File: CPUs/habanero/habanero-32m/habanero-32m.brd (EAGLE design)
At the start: 63.4 x 25.4 mm, 38 parts, among them IC1 PIC32MX564F128H-80I/PT

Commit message: esto solo fue una prueba
rutee una inea dummy
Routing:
- net BUSON: track 9.04 -> 16.6 mm
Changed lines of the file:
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@@
 <?xml version="1.0" encoding="utf-8"?>
 <!DOCTYPE eagle SYSTEM "eagle.dtd">
-<eagle version="6.2">
+<eagle version="6.4">
 <drawing>
 <settings>
@@
 </class>
 </classes>
-<designrules>
+<designrules name="default">
 <description language="de">&lt;b&gt;EAGLE Design Rules&lt;/b&gt;
 &lt;p&gt;
@@
 <wire x1="18.4912" y1="8.128" x2="17.075" y2="8.128" width="0.2032" layer="1"/>
 <wire x1="17.075" y1="8.128" x2="17.004" y2="8.199" width="0.2032" layer="1"/>
-<wire x1="20.5" y1="11.75" x2="44.548625" y2="17.614390625" width="0" layer="19" extent="1-1"/>
+<wire x1="20.5" y1="11.75" x2="25.6032" y2="11.75" width="0.4064" layer="1"/>
+<wire x1="25.6032" y1="11.75" x2="25.6032" y2="14.224" width="0.4064" layer="1"/>
+<wire x1="25.6032" y1="14.224" x2="44.548625" y2="17.614390625" width="0" layer="19" extent="1-16"/>
 </signal>
 <signal name="VBUS">

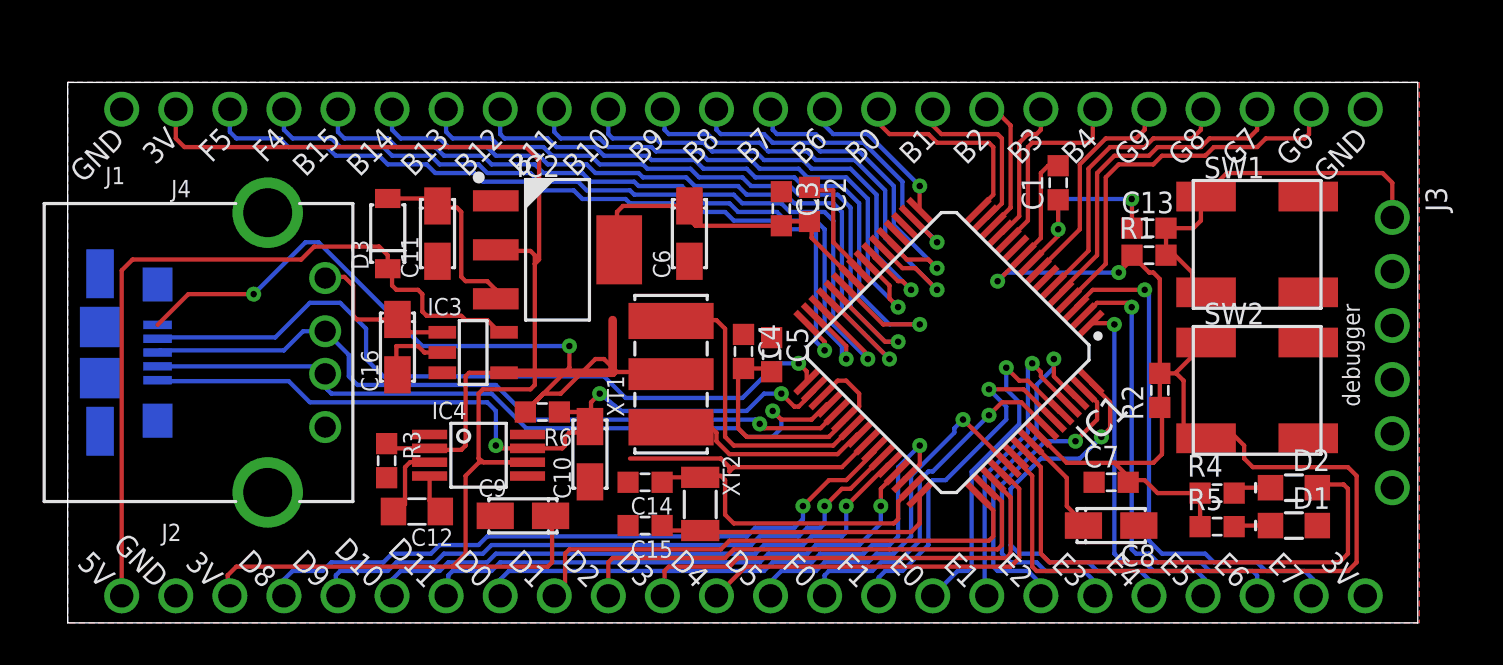
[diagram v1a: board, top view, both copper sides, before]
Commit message: modificaciones en esquematico
- se cambiaron los pin headers de 24 a 23 posiciones, para dejar mas
espacio libre al conector usb on-the-go,
- se corrigio un error de conexion en el conector para el pickit3
-se generaron nuevos modelos ya con pin headers
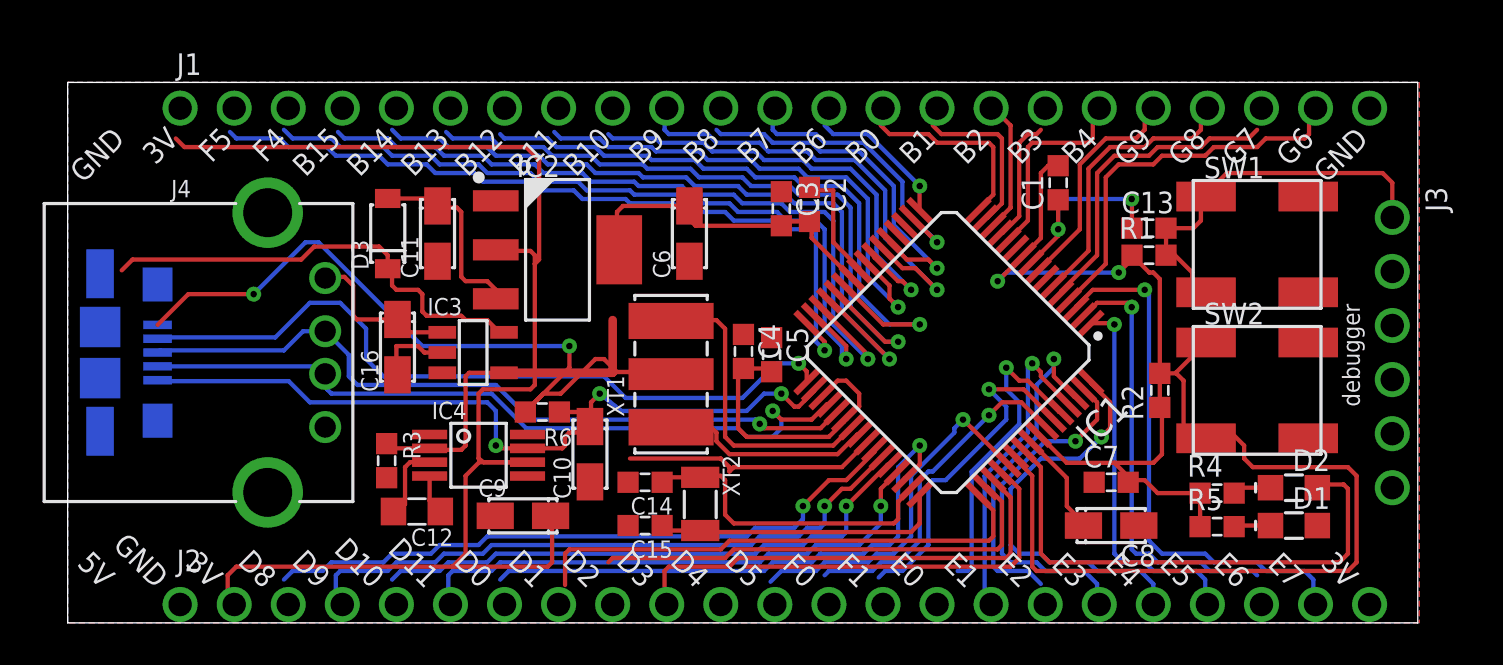
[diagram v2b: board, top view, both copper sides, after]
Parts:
- J1, J2: device wurth-pin-socket-headers:PHSP254P6096X254X1154-24S -> wurth-pin-socket-headers:PHSP254P5842X254X1154-23S
- moved J2 2.77 mm to (5.28, 0.86)
- moved J1 2.74 mm to (5.28, 24.2)
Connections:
- net +3V3: now also J3.2; no longer J2.24, J3.3
- net GND: now also J3.3; no longer J1.24, J3.2
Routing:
- net +5V: track 36.6 -> 21.3 mm
- net E0: track 16.6 -> 14.7 mm
- net D4: track 19.4 -> 17.5 mm
- net D2: track 23.5 -> 21.9 mm
- net +3V3: track 132.7 -> 131.2 mm
- net B12: track 31.4 -> 30.2 mm
- net B10: track 22.5 -> 21.4 mm
- net B15: track 36.5 -> 35.5 mm
- net B13: track 33.0 -> 31.9 mm
- net F5: track 37.9 -> 36.8 mm
- net B11: track 25.5 -> 24.4 mm
- net B14: track 35.5 -> 34.5 mm
- net F0: track 16.9 -> 15.9 mm
- net G7: track 15.7 -> 14.7 mm
- net E6: track 21.3 -> 20.4 mm
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
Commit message: modify resonator part
unrute all
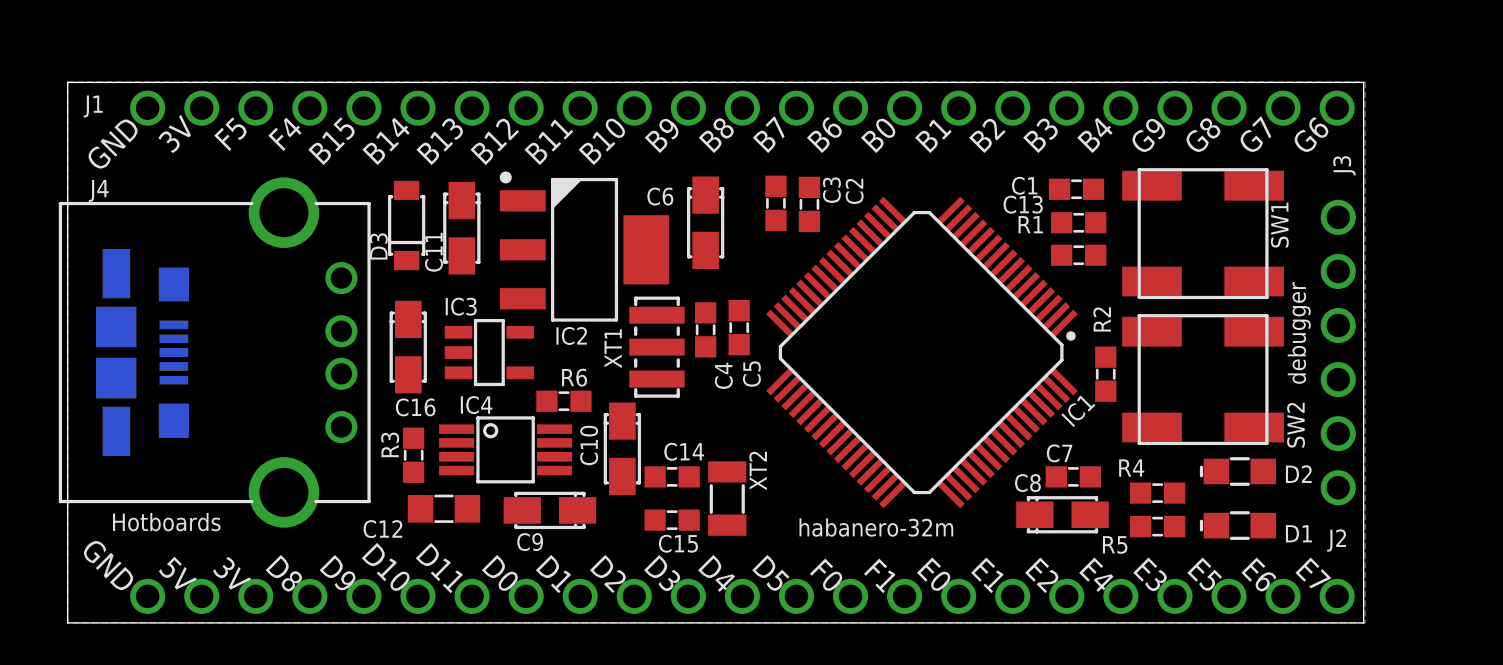
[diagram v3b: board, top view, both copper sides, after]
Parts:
- XT1: value 8MHz -> (none); device abracon-resonators:CERAMIC740X340-3N -> abracon-resonators:CERAMIC460X200-3N
- moved C13 3.31 mm to (47.5, 18.8)
- moved R1 3.30 mm to (47.5, 17.3)
- moved R4 2.79 mm to (51.2, 6.10)
- moved R5 2.79 mm to (51.2, 4.52)
- moved D2 2.65 mm to (55.1, 7.11)
- moved R2 2.65 mm to (48.8, 11.7)
- moved SW1 2.59 mm to (53.3, 18.3)
- moved SW2 2.59 mm to (53.3, 11.4)
- moved D1 2.54 mm to (55.1, 4.57)
- moved J3 2.54 mm to (59.7, 19.1)
- moved C8 2.34 mm to (46.7, 5.08)
- moved C4 2.05 mm to (30.0, 13.8)
- moved C5 1.98 mm to (31.5, 13.9)
- moved C7 1.80 mm to (47.2, 6.86)
- moved J2 1.57 mm to (3.76, 1.24)
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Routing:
- net +3V3: track 131.2 -> 0.00 mm, vias 2 -> 0
- net GND: track 66.0 -> 0.00 mm, vias 4 -> 0
- net BTN: track 41.2 -> 0.00 mm
- net VBUS: track 38.4 -> 0.00 mm, vias 3 -> 0
- net F5: track 36.8 -> 0.00 mm, vias 1 -> 0
- net F4: track 36.6 -> 0.00 mm, vias 1 -> 0
- net B15: track 35.5 -> 0.00 mm, vias 1 -> 0
- net D-: track 35.3 -> 0.00 mm, vias 1 -> 0
- net ID: track 35.2 -> 0.00 mm, vias 1 -> 0
- net D+: track 35.1 -> 0.00 mm, vias 1 -> 0
- net B14: track 34.5 -> 0.00 mm, vias 1 -> 0
- net B13: track 31.9 -> 0.00 mm, vias 1 -> 0
- net D8: track 30.7 -> 0.00 mm, vias 1 -> 0
- net B12: track 30.2 -> 0.00 mm, vias 1 -> 0
- net D9: track 29.3 -> 0.00 mm, vias 1 -> 0
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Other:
- board size 63.4 x 25.4 mm -> 60.9 x 25.4 mm
- board text added: "Hotboards"
- board text added: "habanero-32m"
